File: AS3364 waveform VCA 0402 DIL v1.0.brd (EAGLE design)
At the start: 41.3 x 16.2 mm, 41 parts, among them IC1 TL072JD, IC2 TL072JD

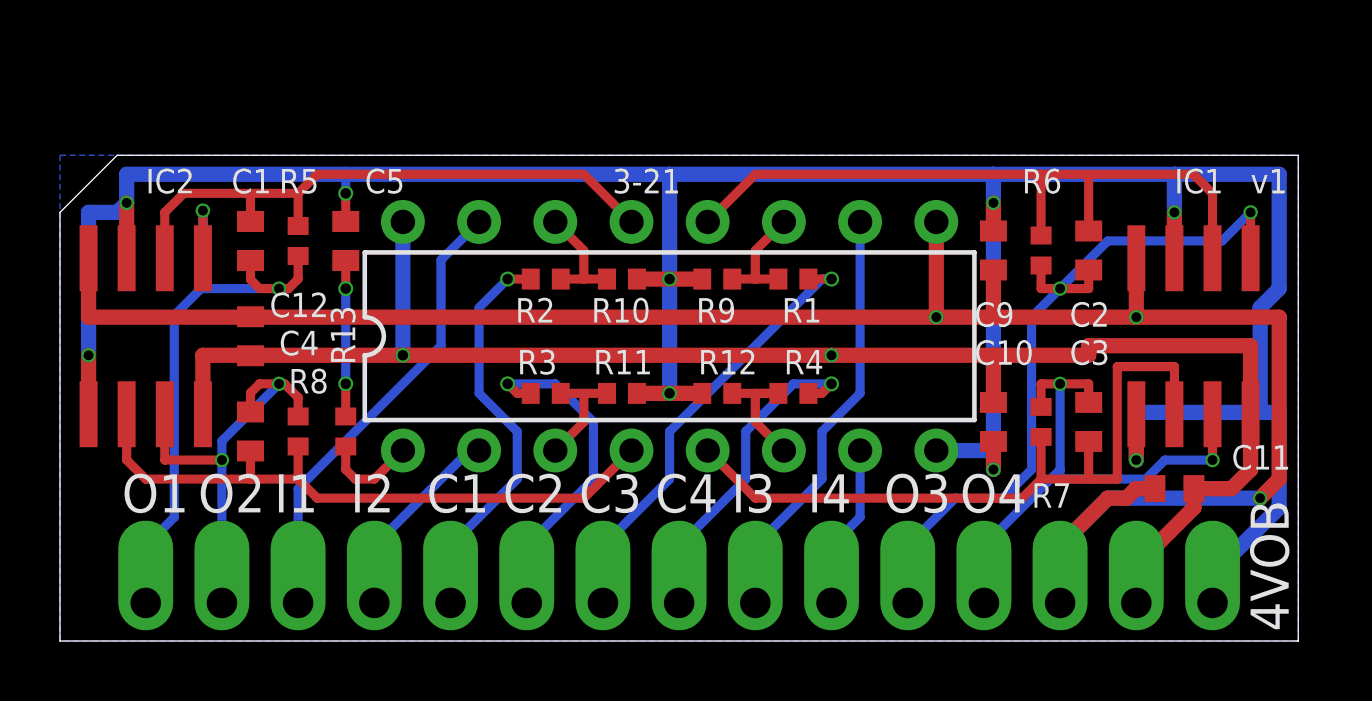
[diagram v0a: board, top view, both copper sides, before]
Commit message: AS3364 based waveshape mixer
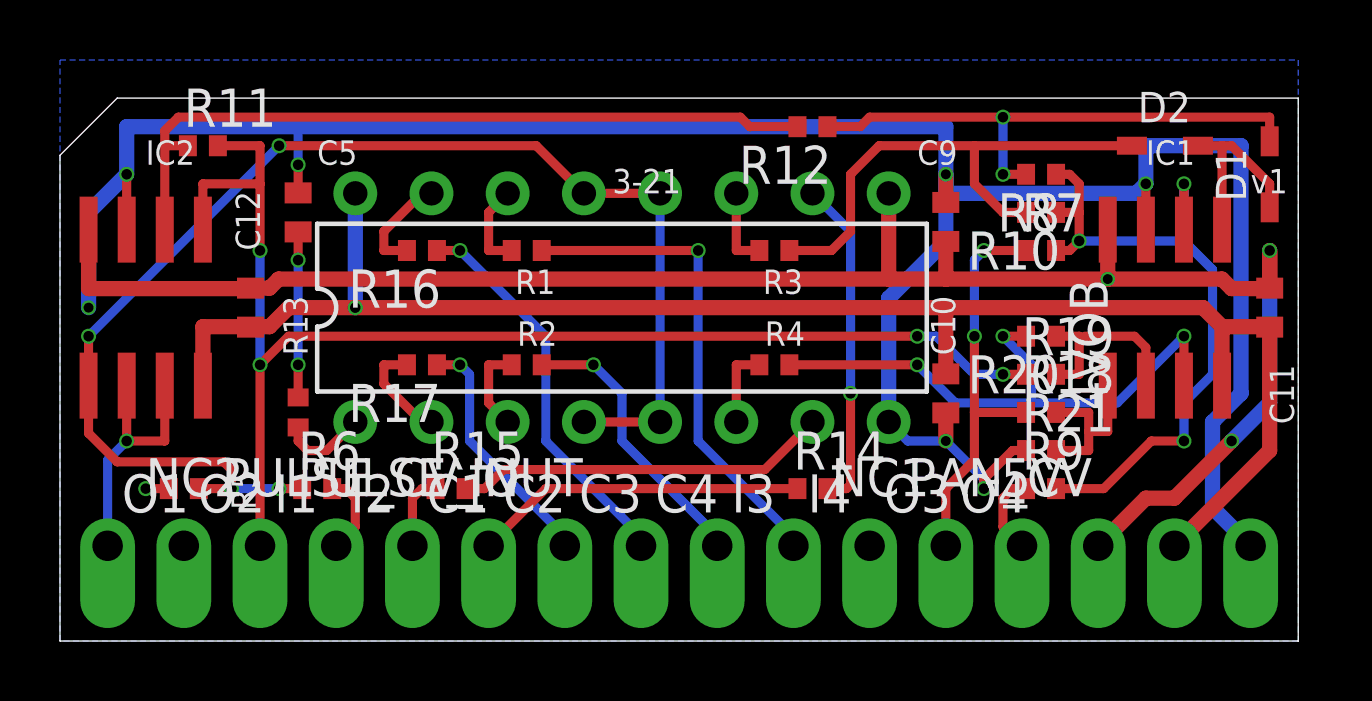
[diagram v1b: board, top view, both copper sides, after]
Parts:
- removed C1, C2, C3, C4: 33pF, rcl:C0402
- removed CV1, CV2, CV3, CV4, IN1, IN2, IN3, IN4, OUT1, OUT2, OUT3, OUT4: (no value), joakim:SIP-PIN01-1J
- added -5V, NC1, NC2, OUT, PAN_CV, PULSE_CV_OUT, PULSE_IN, SAW, SUB1, SUB1_CV, SUB2, SUB2_CV, TRI: (no value), joakim:SIP-PIN01-1J
- added D1, D2: (no value), joakim:SOD323J
- added R14, R15, R16, R17: 47k, rcl:R0402
- added R18, R19: 25k, rcl:R0402
- added R20, R21: 20k, rcl:R0402
- R10, R8: value 47k -> 20k
- R11, R7: value 47k -> 25k
- R12: value 47k -> 10k
- R9: value 47k -> 50k
- moved R8 26.2 mm to (32.7, 15.6), turned to 180 degrees
- moved R6 25.4 mm to (8.57, 5.08), turned to 0 degrees
- moved R11 16.2 mm to (4.76, 16.5), turned to 0 degrees
- moved R10 14.1 mm to (32.7, 14.3)
- moved R9 12.9 mm to (32.7, 5.08)
- moved R12 9.44 mm to (25.1, 17.1), turned to 180 degrees
- moved R5 9.09 mm to (4.13, 5.08), turned to 0 degrees
- moved R3 8.99 mm to (23.8, 13.0), turned to 180 degrees
- moved R1 8.94 mm to (15.6, 13.0)
- moved C11 6.82 mm to (40.3, 11.1), turned to 270 degrees
- moved R7 5.71 mm to (32.7, 13.0), turned to 0 degrees
- moved R2 2.93 mm to (15.6, 9.21), turned to 180 degrees
- moved +12V 2.29 mm to (37.1, 3.17), turned to 0 degrees
- moved -12V 2.29 mm to (34.6, 3.17), turned to 0 degrees
- moved GND 2.29 mm to (39.7, 3.17), turned to 0 degrees
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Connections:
- removed net CV1: CV1.1, R2.1
- removed net CV2: CV2.1, R3.1
- removed net CV2_IN: DA2.3, R11.2, R3.2
- removed net CV3: CV3.1, R1.1
- removed net CV4: CV4.1, R4.1
- removed net IN1: DA2.15, IN1.1
- removed net IN2: DA2.2, IN2.1
- removed net IN3: DA2.10, IN3.1
- removed net IN4: DA2.7, IN4.1
- removed net N$1: C4.1, DA2.4, IC2.6, R8.1
- removed net N$10: DA2.6, R12.2, R4.2
- removed net N$12: DA2.11, R1.2, R9.2
- removed net N$21: DA2.14, R10.2, R2.2
- removed net N$3: C3.1, DA2.5, IC1.6, R7.1
- removed net N$5: C2.1, DA2.12, IC1.2, R6.1
- removed net N$7: C1.1, DA2.13, IC2.2, R5.1
- removed net OUT1: C1.2, IC2.1, OUT1.1, R5.2
- removed net OUT2: C4.2, IC2.7, OUT2.1, R8.2
- removed net OUT3: C2.2, IC1.1, OUT3.1, R6.2
- removed net OUT4: C3.2, IC1.7, OUT4.1, R7.2
- new net -5V: -5V.1, R9.1
- new net MIX_BUS: DA2.12, DA2.13, DA2.4, DA2.5, IC2.5, R5.2, R6.1
- new net N$11: IC1.5, R18.2, R21.2
- new net N$15: IC1.6, R19.2, R20.1
- new net N$18: IC2.2, R11.1, R12.2
- new net N$19: D1.2, R12.1, R8.2
- new net N$6: D1.1, D2.2, IC1.1
- new net N$8: IC1.2, R10.1, R7.2, R8.1, R9.2
- new net OUT: IC2.6, IC2.7, OUT.1
- new net PAN_CV: PAN_CV.1, R18.1, R7.1
- new net PULSE_CV: IC2.1, PULSE_CV_OUT.1, R11.2, R19.1
- new net PULSE_IN: PULSE_IN.1, R6.2
- new net SAW: R15.1, SAW.1
- new net SAW_CV: IC1.7, R20.2, R4.1
- new net SAW_CV_IN: DA2.6, R4.2
- new net SAW_IN: DA2.7, R15.2
- new net SUB1: R16.1, SUB1.1
- new net SUB1_CV: R1.1, SUB1_CV.1
- new net SUB1_CV_IN: DA2.14, R1.2
- new net SUB1_IN: DA2.15, R16.2
- new net SUB2: R17.1, SUB2.1
- new net SUB2_CV: R2.1, SUB2_CV.1
- new net SUB2_CV_IN: DA2.3, R2.2
- new net SUB2_IN: DA2.2, R17.2
- new net TRI: R14.1, TRI.1
- new net TRI_CV: D2.1, R10.2, R3.1
- new net TRI_CV_IN: DA2.11, R3.2
- new net TRI_IN: DA2.10, R14.2
- net GND: now also R21.1, R5.1; no longer IC1.5, IC2.5, R10.1, R11.1, R12.1, R9.1
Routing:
- net MIX_BUS: track 0.00 -> 45.1 mm, vias 0 -> 4
- net PULSE_CV: track 0.00 -> 44.6 mm, vias 0 -> 4
- net N$18: track 0.00 -> 25.5 mm
- net OUT3: track 25.4 -> 0.00 mm, vias 2 -> 0
- net N$3: track 24.5 -> 0.00 mm
- net OUT1: track 23.8 -> 0.00 mm, vias 2 -> 0
- net N$5: track 23.8 -> 0.00 mm
- net N$8: track 0.00 -> 23.8 mm, vias 0 -> 3
- net N$1: track 21.6 -> 0.00 mm
- net N$7: track 20.3 -> 0.00 mm
- net SAW_CV: track 0.00 -> 19.6 mm, vias 0 -> 3
- net OUT4: track 18.5 -> 0.00 mm, vias 2 -> 0
- net N$19: track 0.00 -> 18.4 mm, vias 0 -> 2
- net TRI_CV: track 0.00 -> 17.4 mm
- net GND: track 102.3 -> 85.3 mm, vias 9 -> 8
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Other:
- board size 41.3 x 16.2 mm -> 41.3 x 18.1 mm
- board text added: "Quad linear VCA"
- board text removed: "Quad lin inv VCA"

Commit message: Finished waveshape mixer and fixed a serious bug
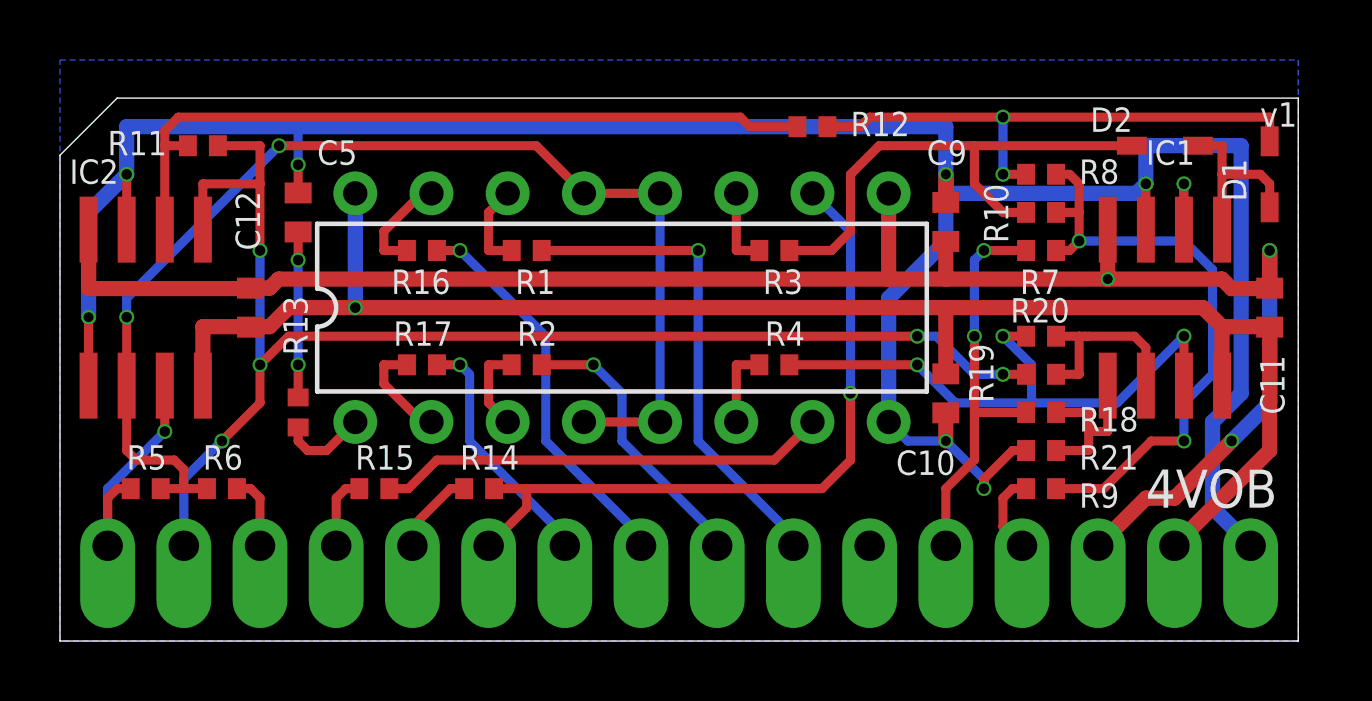
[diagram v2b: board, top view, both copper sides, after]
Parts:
- removed NC2: (no value), joakim:SIP-PIN01-1J
- added TRI_DIRECT: (no value), joakim:SIP-PIN01-1J
- moved R14 11.1 mm to (14.0, 5.08)
- moved R6 3.17 mm to (5.40, 5.08)
- moved R15 2.54 mm to (10.5, 5.08)
- moved SAW 2.54 mm to (9.21, 3.17)
- moved PULSE_CV_OUT 2.54 mm to (4.13, 3.17)
- moved PULSE_IN 2.54 mm to (6.67, 3.17)
- moved TRI 2.54 mm to (11.7, 3.17)
- moved R5 1.27 mm to (2.86, 5.08)
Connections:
- net GND: now also IC2.5; no longer R5.1
- net MIX_BUS: now also IC2.6; no longer IC2.5
- net OUT: now also R5.1; no longer IC2.6
- net TRI_IN: now also TRI_DIRECT.1
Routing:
- net TRI_IN: track 11.1 -> 24.1 mm
- net TRI: track 11.1 -> 2.88 mm
- net MIX_BUS: track 45.1 -> 40.1 mm, vias 4 -> 2
- net SAW_IN: track 12.5 -> 15.0 mm
- net GND: track 85.3 -> 87.1 mm, vias 8 -> 7
- net PULSE_CV: track 44.6 -> 45.7 mm, vias 4 -> 5
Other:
- board text added: "1"
- board text added: "1C"
- board text added: "2"
- board text added: "2C"
- board text added: "5V"
- board text added: "CV"
- board text added: "IN"
- board text added: "O"
- board text added: "Pulse"
- board text added: "SW"
- board text added: "Sub osc"
- board text added: "TD"
- board text added: "TR"
- board text added: "Wave- shape mixer"
- board text removed: "3-21"
- board text removed: "C1"
- board text removed: "C2"
- board text removed: "C3"
- board text removed: "C4"
- board text removed: "I1"
- board text removed: "I2"
- board text removed: "I3"
- board text removed: "I4"
- board text removed: "O1"
- board text removed: "O2"
- board text removed: "O3"
- board text removed: "O4"
- board text removed: "Quad linear VCA"

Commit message: Checked most things, changed CV input resistors, added cap to mixer output
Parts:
- added C1: 33pF, rcl:C0402
- R1, R2: value 47k -> 33k
- R3, R4: value 47k -> 22k
- moved R3 8.26 mm to (15.6, 13.0), turned to 0 degrees
- moved R4 8.26 mm to (15.6, 9.21), turned to 0 degrees
- moved R1 3.18 mm to (18.7, 13.0)
- moved R2 3.18 mm to (18.7, 9.21)
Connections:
- removed net SAW_CV_IN: DA2.6, R4.2
- removed net TRI_CV_IN: DA2.11, R3.2
- net GND: now also R3.1, R4.1
- net MIX_BUS: now also C1.2
- net OUT: now also C1.1
- net SAW_CV: now also DA2.6; no longer R4.1
- net SUB1_CV_IN: now also R3.2
- net SUB2_CV_IN: now also R4.2
- net TRI_CV: now also DA2.11; no longer R3.1
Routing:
- net GND: track 87.1 -> 102.3 mm, vias 7 -> 9
- net MIX_BUS: track 40.1 -> 44.7 mm, vias 2 -> 3
- net OUT: track 8.62 -> 12.5 mm, vias 1 -> 2
- net SUB1_CV: track 16.4 -> 13.2 mm
- net TRI_CV_IN: track 2.67 -> 0.00 mm
- net SAW_CV_IN: track 2.67 -> 0.00 mm
- net TRI_CV: track 17.4 -> 19.9 mm
- net SAW_CV: track 19.6 -> 22.2 mm
- net SUB2_CV_IN: track 2.94 -> 5.24 mm
- net SUB1_CV_IN: track 2.94 -> 5.24 mm
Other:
- board text added: "AS3364"

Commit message: Almost finished bom/cpl
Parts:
- removed +12V, -12V, -5V, GND, NC1, OUT, PAN_CV, PULSE_CV_OUT, PULSE_IN, SAW, SUB1, SUB1_CV, SUB2, SUB2_CV, TRI, TRI_DIRECT: (no value), joakim:SIP-PIN01-1J
- added SV1, SV2: (no value), joakim:SIP-PIN08-1J
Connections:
- net +12V: now also SV2.7; no longer +12V.1
- net -12V: now also SV2.6; no longer -12V.1
- net -5V: now also SV2.5; no longer -5V.1
- net GND: now also SV2.8; no longer GND.1
- net OUT: now also SV1.1; no longer OUT.1
- net PAN_CV: now also SV2.4; no longer PAN_CV.1
- net PULSE_CV: now also SV1.2; no longer PULSE_CV_OUT.1
- net PULSE_IN: now also SV1.3; no longer PULSE_IN.1
- net SAW: now also SV1.4; no longer SAW.1
- net SUB1: now also SV1.8; no longer SUB1.1
- net SUB1_CV: now also SV2.2; no longer SUB1_CV.1
- net SUB2: now also SV1.7; no longer SUB2.1
- net SUB2_CV: now also SV2.1; no longer SUB2_CV.1
- net TRI: now also SV1.5; no longer TRI.1
- net TRI_IN: now also SV1.6; no longer TRI_DIRECT.1
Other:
- board text added: "-5V"
- board text removed: "5V"
